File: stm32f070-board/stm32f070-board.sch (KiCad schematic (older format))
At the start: 0 parts

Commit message: drafted the 3v3 power supply section using LD3950
Signed-off-by: suyash <in.suyash@gmail.com>
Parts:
- added C? (x2): C, symbol Device:C
- added D?: LED, symbol Device:LED
- added J?: USB_B_Micro, symbol Connector:USB_B_Micro
- added R?: R, symbol Device:R
- added VR?: LD39050PU33R, symbol stm32f070-board:LD39050PU33R
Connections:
- new net: C?.1, J?.1 (VBUS), VR?.1 (EN), VR?.6 (VIN)
- new net: D?.2 (A), R?.2
- new net GND: C?.2, C?.2, D?.1 (K), J?.5 (GND), J?.6 (Shield), VR?.2 (GND), VR?.7 (GND)
- new net VCC: C?.1, R?.1, VR?.4 (VOUT)
- no-connect marks 0 -> 2
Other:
- note added: "Check if the USB shield connection goes to ground\n"
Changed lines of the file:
@@
 EESchema Schematic File Version 4
+LIBS:stm32f070-board-cache
 EELAYER 26 0
 EELAYER END
@@
 Comment4 "Author: Suyash Singh B."
 $EndDescr
+$Comp
+L stm32f070-board:LD39050PU33R VR?
+U 1 1 5D7A09D8
+P 2650 1500
+F 0 "VR?" H 2650 1920 50  0000 C CNN
+F 1 "LD39050PU33R" H 2650 1829 50  0000 C CNN
+F 2 "" H 2650 1550 50  0001 C CNN
+F 3 "" H 2650 1550 50  0001 C CNN
+	1    2650 1500
+	1    0    0    -1
+$EndComp
+$Comp
+L Connector:USB_B_Micro J?
+U 1 1 5D7A0AEB
+P 1000 1550
+F 0 "J?" H 1055 2017 50  0000 C CNN
+F 1 "USB_B_Micro" H 1055 1926 50  0000 C CNN
+F 2 "" H 1150 1500 50  0001 C CNN
+F 3 "~" H 1150 1500 50  0001 C CNN
+	1    1000 1550
+	1    0    0    -1
+$EndComp
+$Comp
+L Device:C C?
+U 1 1 5D7A0BBE
+P 1850 1650
+F 0 "C?" H 1965 1696 50  0000 L CNN
+F 1 "C" H 1965 1605 50  0000 L CNN
+F 2 "" H 1888 1500 50  0001 C CNN
+F 3 "~" H 1850 1650 50  0001 C CNN
+	1    1850 1650
+	1    0    0    -1
+$EndComp
+$Comp
+L Device:R R?
+U 1 1 5D7A0C0E
+P 3500 1500
+F 0 "R?" H 3570 1546 50  0000 L CNN
+F 1 "R" H 3570 1455 50  0000 L CNN
+F 2 "" V 3430 1500 50  0001 C CNN
+F 3 "~" H 3500 1500 50  0001 C CNN
+	1    3500 1500
+	1    0    0    -1
+$EndComp
+$Comp
+L Device:LED D?
+U 1 1 5D7A0C7B
+P 3500 1900
+F 0 "D?" V 3538 1783 50  0000 R CNN
+F 1 "LED" V 3447 1783 50  0000 R CNN
+F 2 "" H 3500 1900 50  0001 C CNN
+F 3 "~" H 3500 1900 50  0001 C CNN
+	1    3500 1900
+	0    -1   -1   0
+$EndComp
+$Comp
+L Device:C C?
+U 1 1 5D7A0CB9
+P 3950 1650
+F 0 "C?" H 4065 1696 50  0000 L CNN
+F 1 "C" H 4065 1605 50  0000 L CNN
+F 2 "" H 3988 1500 50  0001 C CNN
+F 3 "~" H 3950 1650 50  0001 C CNN
+	1    3950 1650
+	1    0    0    -1
+$EndComp
+Wire Wire Line
+	3000 1350 3500 1350
+Wire Wire Line
+	3500 1350 3950 1350
+Connection ~ 3500 1350
+Wire Wire Line
+	3500 1650 3500 1750
+Wire Wire Line
+	3500 2050 3000 2050
+Wire Wire Line
+	1000 2050 1000 1950
+Wire Wire Line
+	1300 1350 1850 1350
+Wire Wire Line
+	1850 1500 1850 1350
+Connection ~ 1850 1350
+Wire Wire Line
+	1850 1350 2200 1350
+Wire Wire Line
+	3950 1350 3950 1500
+Wire Wire Line
+	3500 2050 3950 2050
+Wire Wire Line
+	3950 2050 3950 1800
+Connection ~ 3500 2050
+$Comp
+L power:GND #PWR?
+U 1 1 5D7A1575
+P 3950 2100
+F 0 "#PWR?" H 3950 1850 50  0001 C CNN
+F 1 "GND" H 3955 1927 50  0000 C CNN
+F 2 "" H 3950 2100 50  0001 C CNN
+F 3 "" H 3950 2100 50  0001 C CNN
+	1    3950 2100
+	1    0    0    -1
+$EndComp
+Wire Wire Line
+	3000 1750 3000 2050
+Connection ~ 3000 2050
+Wire Wire Line
+	1000 2050 1850 2050
+Wire Wire Line
+	1850 1800 1850 2050
+Connection ~ 1850 2050
+Wire Wire Line
+	1850 2050 3000 2050
+Wire Wire Line
+	3950 2100 3950 2050
+Connection ~ 3950 2050
+$Comp
+L power:VCC #PWR?
+U 1 1 5D7A1B6E
+P 3950 1250
+F 0 "#PWR?" H 3950 1100 50  0001 C CNN
+F 1 "VCC" H 3967 1423 50  0000 C CNN
+F 2 "" H 3950 1250 50  0001 C CNN
+F 3 "" H 3950 1250 50  0001 C CNN
+	1    3950 1250
+	1    0    0    -1
+$EndComp
+Wire Wire Line
+	3950 1350 3950 1250
+Connection ~ 3950 1350
+Wire Wire Line
+	2300 1550 2200 1550
+Wire Wire Line
+	2200 1550 2200 1350
+Connection ~ 2200 1350
+Wire Wire Line
+	2200 1350 2300 1350
+Wire Wire Line
+	900  1950 900  2050
+Wire Wire Line
+	900  2050 1000 2050
+Connection ~ 1000 2050
+Text Notes 700  2250 0    50   ~ 0
+Check if the USB shield connection goes to ground\n
+NoConn ~ 3000 1550
+NoConn ~ 4200 3200
 $EndSCHEMATC

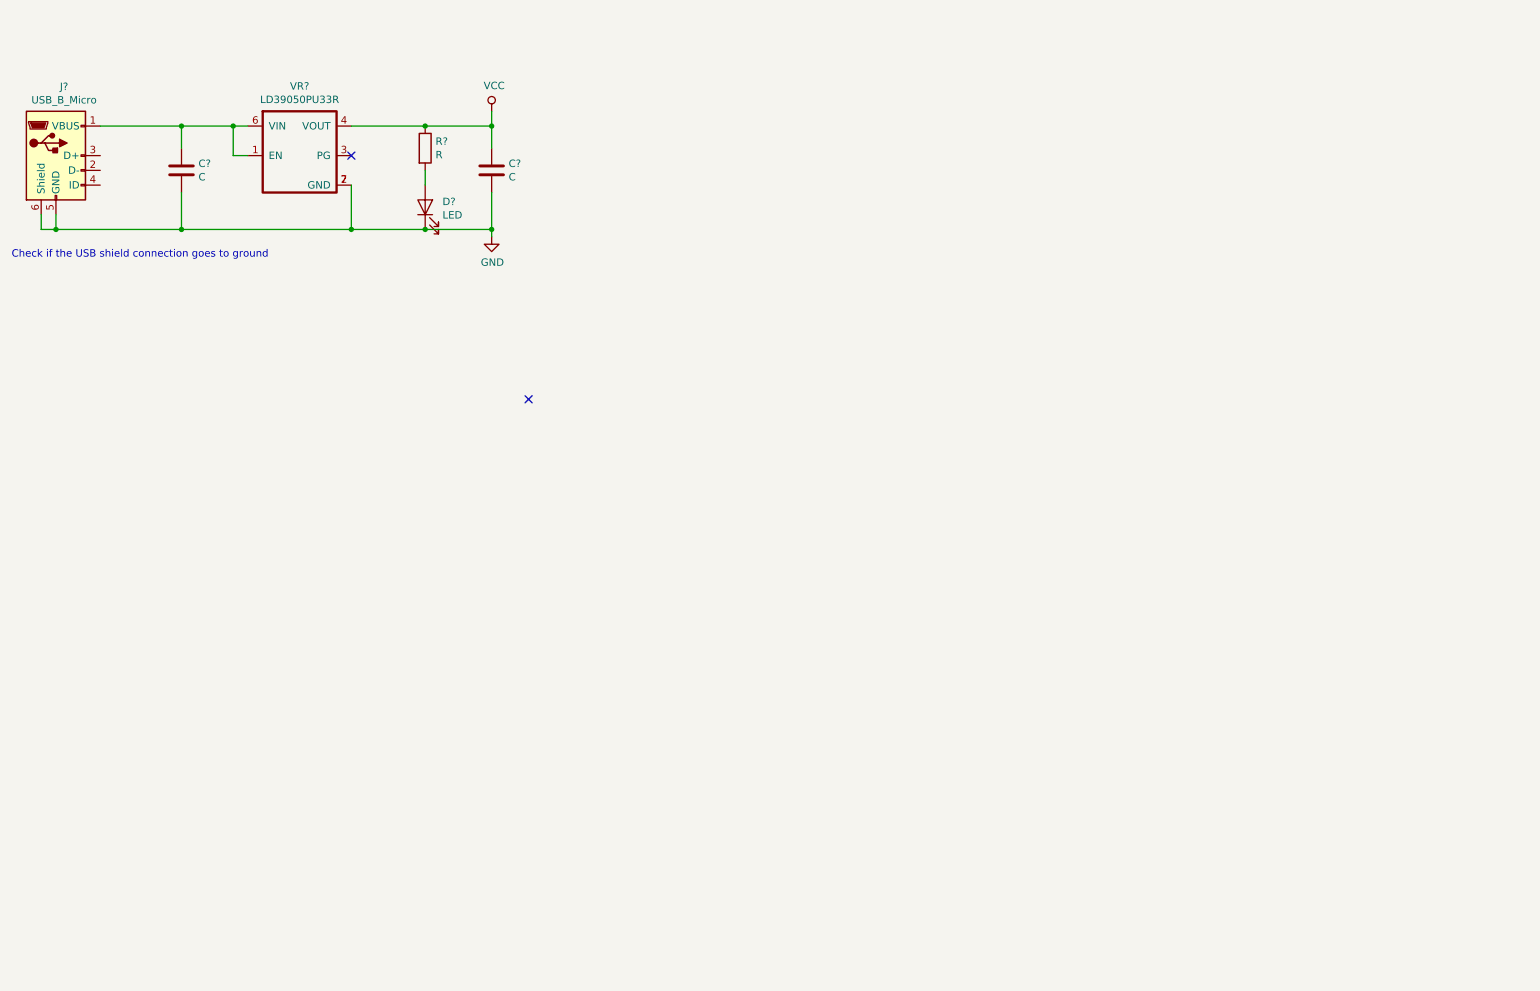
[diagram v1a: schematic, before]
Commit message: drafted schematic using STM32FO mcu symbol, added debug
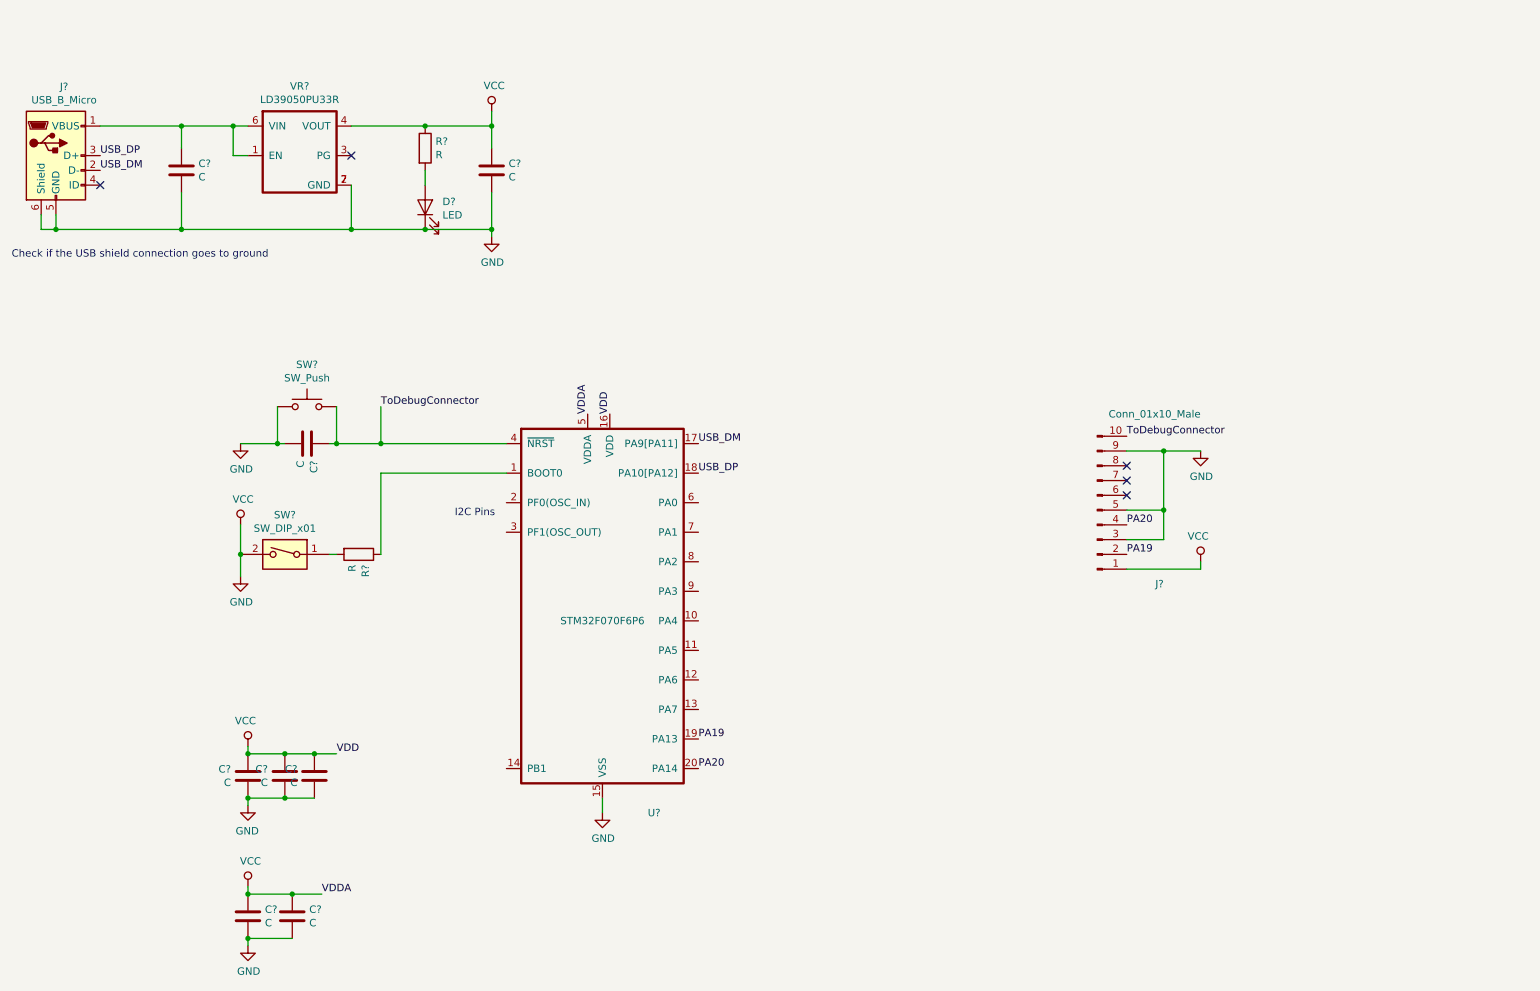
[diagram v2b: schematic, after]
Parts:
- added C? (x6): C, symbol Device:C
- added J?: Conn_01x10_Male, symbol Connector:Conn_01x10_Male
- added R?: R, symbol Device:R
- added SW?: SW_DIP_x01, symbol Switch:SW_DIP_x01
- added SW?: SW_Push, symbol Switch:SW_Push
- added U?: STM32F070F6P6, symbol stm32f070-board:STM32F070F6P6
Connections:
- net VCC is gone; now on net GND: C?.1, R?.1, VR?.4 (VOUT)
- net GND: now also C?.1, C?.1, C?.1, C?.1, C?.1, C?.2, C?.2, C?.2, C?.2, C?.2, C?.2, J?.1 (Pin_1), J?.3 (Pin_3), J?.5 (Pin_5), J?.9 (Pin_9), SW?.1, SW?.2, U?.15 (VSS), U?.16 (VDD), U?.5 (VDDA)
- net USB_DM: now reaches J?.2 (D-)
- net USB_DM: now also U?.17 (PA9[PA11])
- net USB_DP: now reaches J?.3 (D+)
- net USB_DP: now also U?.18 (PA10[PA12])
- new net: R?.1, U?.1 (BOOT0)
- new net: R?.2, SW?.1
- new net PA19: J?.2 (Pin_2), U?.19 (PA13)
- new net PA20: J?.4 (Pin_4), U?.20 (PA14)
- new net ToDebugConnector: C?.1, J?.10 (Pin_10), SW?.2, U?.4 (~NRST)
- no-connect marks 2 -> 5
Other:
- note added: "I2C Pins\n"

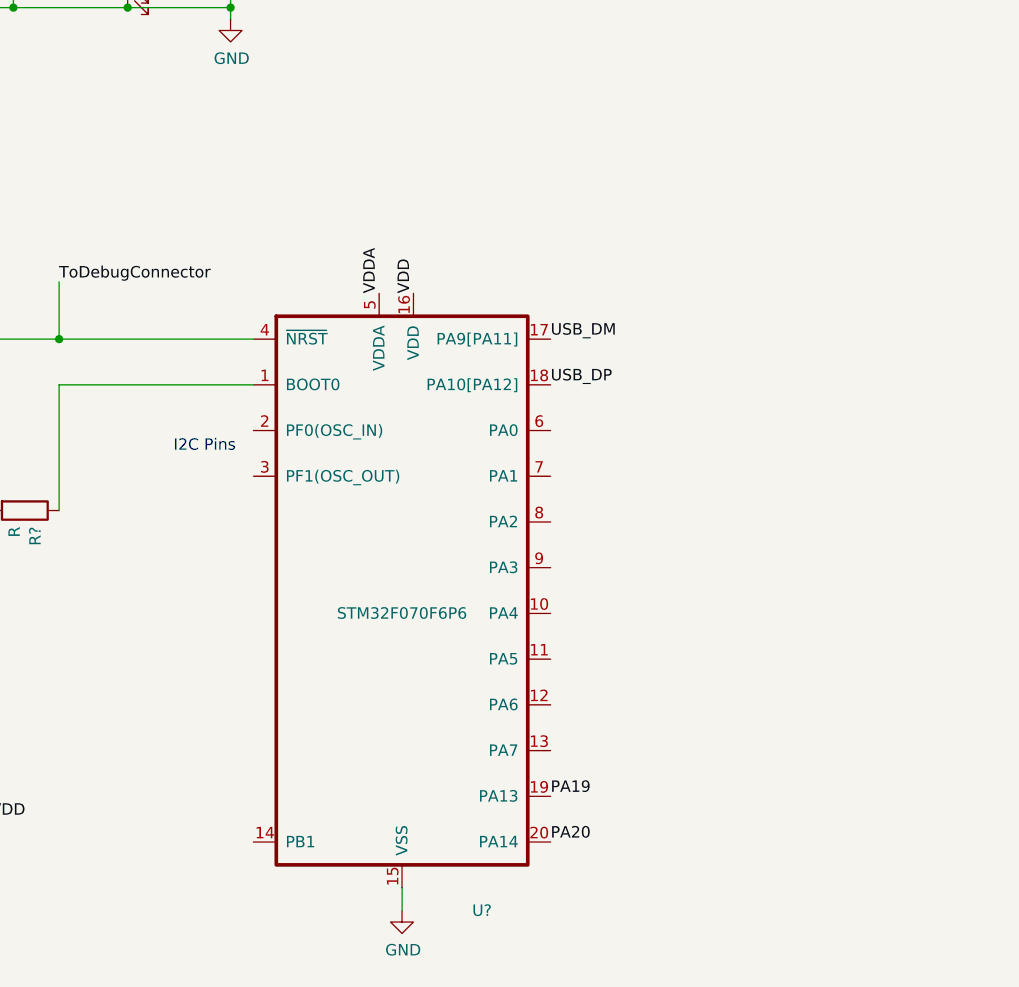
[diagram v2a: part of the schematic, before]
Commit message: added connections for user switch and led
Signed-off-by: suyash <in.suyash@gmail.com>
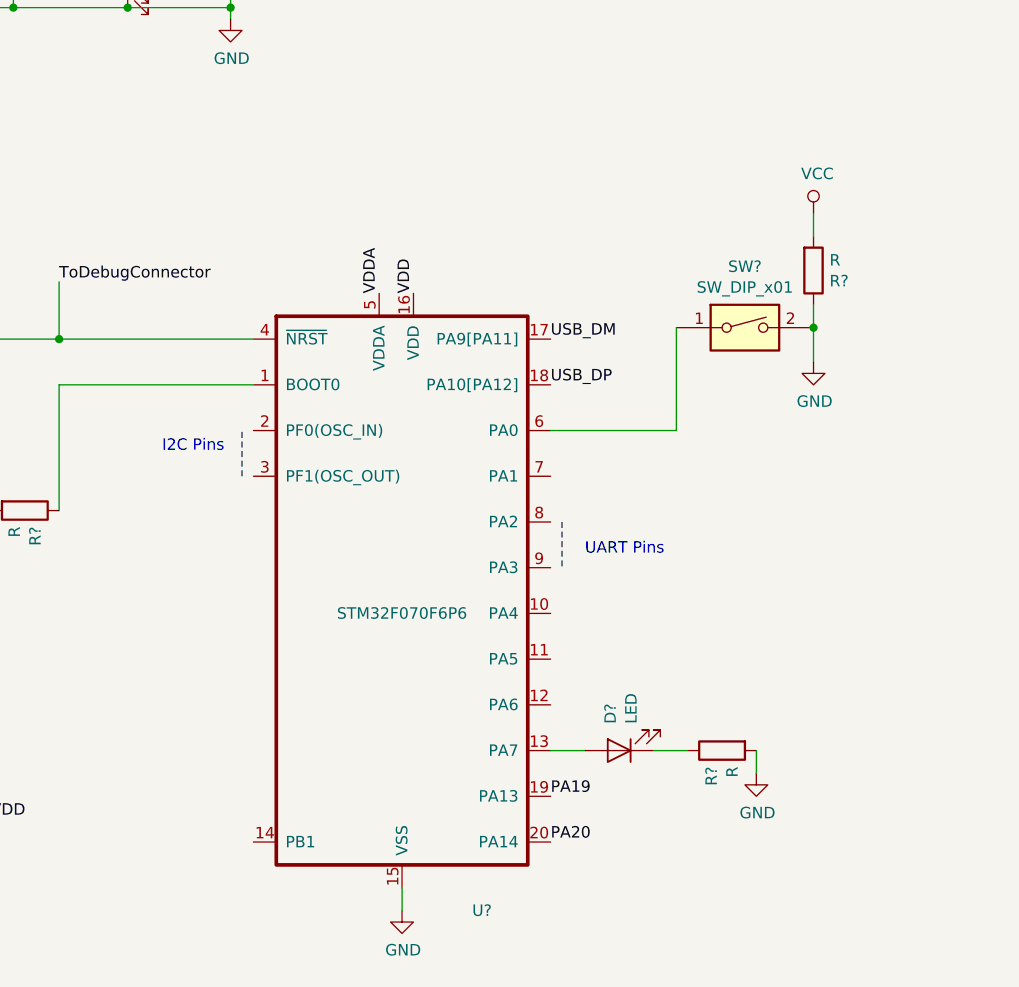
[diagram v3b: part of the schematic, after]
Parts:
- added D?: LED, symbol Device:LED
- added R? (x2): R, symbol Device:R
- added SW?: SW_DIP_x01, symbol Switch:SW_DIP_x01
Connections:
- net GND: now also R?.1, R?.2, R?.2, SW?.2
- net at U?.13 (PA7): now also D?.2 (A)
- net at U?.6 (PA0): now also SW?.1
- new net: D?.1 (K), R?.1
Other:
- note added: "UART Pins\n"
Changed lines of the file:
@@
 	2250 4400 2250 4250
 Connection ~ 2250 4250
-Text Notes 3700 4000 0    50   ~ 0
+Text Notes 3650 4000 0    50   ~ 0
 I2C Pins\n
 $Comp
@@
 Text Label 5350 3700 0    50   ~ 0
 USB_DP
+$Comp
+L Switch:SW_DIP_x01 SW?
+U 1 1 5D7CAFC7
+P 6200 3450
+F 0 "SW?" H 6200 3717 50  0000 C CNN
+F 1 "SW_DIP_x01" H 6200 3626 50  0000 C CNN
+F 2 "" H 6200 3450 50  0001 C CNN
+F 3 "" H 6200 3450 50  0001 C CNN
+	1    6200 3450
+	1    0    0    -1
+$EndComp
+$Comp
+L power:VCC #PWR?
+U 1 1 5D7CB054
+P 6500 2950
+F 0 "#PWR?" H 6500 2800 50  0001 C CNN
+F 1 "VCC" H 6517 3123 50  0000 C CNN
+F 2 "" H 6500 2950 50  0001 C CNN
+F 3 "" H 6500 2950 50  0001 C CNN
+	1    6500 2950
+	1    0    0    -1
+$EndComp
+$Comp
+L Device:R R?
+U 1 1 5D7CB083
+P 6500 3200
+F 0 "R?" H 6570 3246 50  0000 L CNN
+F 1 "R" H 6570 3155 50  0000 L CNN
+F 2 "" V 6430 3200 50  0001 C CNN
+F 3 "~" H 6500 3200 50  0001 C CNN
+	1    6500 3200
+	1    0    0    1
+$EndComp
+Wire Wire Line
+	6500 3050 6500 2950
+Wire Wire Line
+	6500 3450 6500 3350
+$Comp
+L power:GND #PWR?
+U 1 1 5D7CE5CC
+P 6500 3600
+F 0 "#PWR?" H 6500 3350 50  0001 C CNN
+F 1 "GND" H 6505 3427 50  0000 C CNN
+F 2 "" H 6500 3600 50  0001 C CNN
+F 3 "" H 6500 3600 50  0001 C CNN
+	1    6500 3600
+	1    0    0    -1
+$EndComp
+Wire Wire Line
+	6500 3600 6500 3450
+Connection ~ 6500 3450
+Wire Wire Line
+	5350 3900 5900 3900
+Wire Wire Line
+	5900 3900 5900 3450
+Wire Notes Line
+	4000 4100 4000 3900
+Wire Notes Line
+	5400 4300 5400 4500
+Text Notes 5500 4450 0    50   ~ 0
+UART Pins\n
+$Comp
+L Device:LED D?
+U 1 1 5D7D3C44
+P 5650 5300
+F 0 "D?" V 5688 5183 50  0000 R CNN
+F 1 "LED" V 5597 5183 50  0000 R CNN
+F 2 "" H 5650 5300 50  0001 C CNN
+F 3 "~" H 5650 5300 50  0001 C CNN
+	1    5650 5300
+	-1   0    0    1
+$EndComp
+$Comp
+L Device:R R?
+U 1 1 5D7D3F06
+P 6100 5300
+F 0 "R?" H 6170 5346 50  0000 L CNN
+F 1 "R" H 6170 5255 50  0000 L CNN
+F 2 "" V 6030 5300 50  0001 C CNN
+F 3 "~" H 6100 5300 50  0001 C CNN
+	1    6100 5300
+	0    -1   1    0
+$EndComp
+$Comp
+L power:GND #PWR?
+U 1 1 5D7D40BD
+P 6250 5400
+F 0 "#PWR?" H 6250 5150 50  0001 C CNN
+F 1 "GND" H 6255 5227 50  0000 C CNN
+F 2 "" H 6250 5400 50  0001 C CNN
+F 3 "" H 6250 5400 50  0001 C CNN
+	1    6250 5400
+	1    0    0    -1
+$EndComp
+Wire Wire Line
+	6250 5400 6250 5300
+Wire Wire Line
+	5950 5300 5800 5300
+Wire Wire Line
+	5500 5300 5350 5300
 $EndSCHEMATC
